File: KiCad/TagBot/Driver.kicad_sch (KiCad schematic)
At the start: 3 parts, among them U2 ZXBM5210-SP

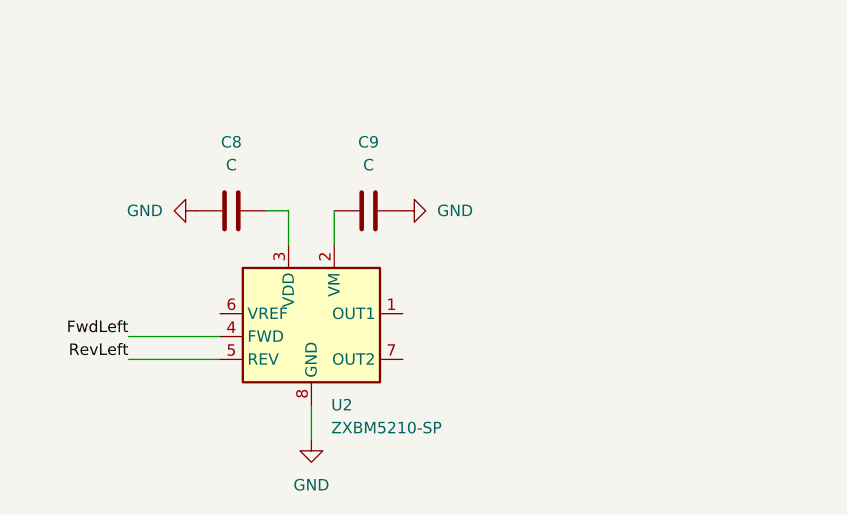
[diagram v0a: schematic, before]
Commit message: kicad and cubeide pin config
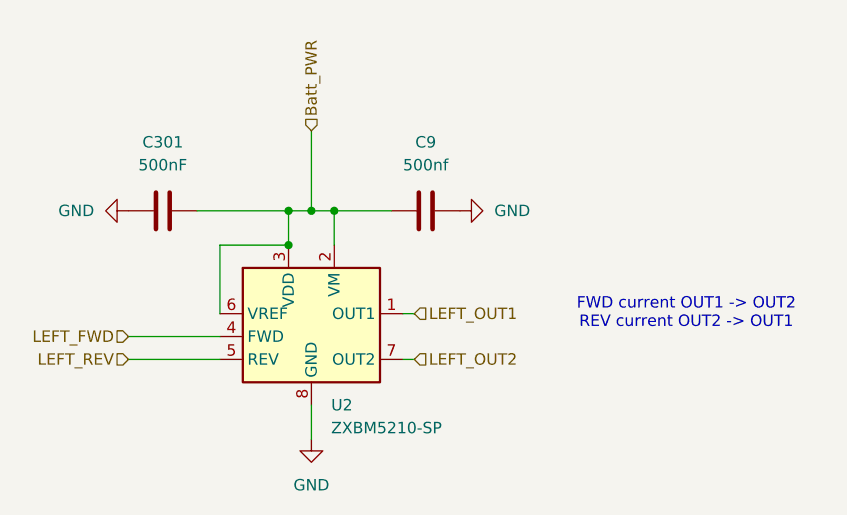
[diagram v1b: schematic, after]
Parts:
- C301: renamed from C8; value C -> 500nF
- C9: value C -> 500nf
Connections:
- net Batt_PWR: now reaches C301.2, U2.3 (VDD)
- net Batt_PWR: now also C9.2, U2.2 (VM), U2.6 (VREF)
- net LEFT_OUT1: now reaches U2.1 (OUT1)
- net LEFT_OUT2: now reaches U2.7 (OUT2)
- net FwdLeft renamed LEFT_FWD
- net RevLeft renamed LEFT_REV
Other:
- note added: "FWD current OUT1 -> OUT2 REV current OUT2 -> OUT1"
- moved on the sheet: C301, C9
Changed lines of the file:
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@@
 	(generator_version "8.0")
 	(paper "A4")
+	(junction
+		(at 138.43 73.66)
+		(diameter 0)
+		(color 0 0 0 0)
+	)
+	(junction
+		(at 143.51 73.66)
+		(diameter 0)
+		(color 0 0 0 0)
+	)
+	(junction
+		(at 140.97 73.66)
+		(diameter 0)
+		(color 0 0 0 0)
+	)
+	(junction
+		(at 138.43 77.47)
+		(diameter 0)
+		(color 0 0 0 0)
+	)
+	(wire
+		(pts
+			(xy 130.81 85.09) (xy 130.81 77.47)
+		)
+		(stroke
+			(width 0)
+			(type default)
+		)
+	)
+	(wire
+		(pts
+			(xy 138.43 73.66) (xy 140.97 73.66)
+		)
+		(stroke
+			(width 0)
+			(type default)
+		)
+	)
 	(wire
 		(pts
@@
 	(wire
 		(pts
+			(xy 152.4 85.09) (xy 151.13 85.09)
+		)
+		(stroke
+			(width 0)
+			(type default)
+		)
+	)
+	(wire
+		(pts
+			(xy 152.4 90.17) (xy 151.13 90.17)
+		)
+		(stroke
+			(width 0)
+			(type default)
+		)
+	)
+	(wire
+		(pts
 			(xy 143.51 73.66) (xy 143.51 77.47)
 		)
@@
 	(wire
 		(pts
+			(xy 130.81 77.47) (xy 138.43 77.47)
+		)
+		(stroke
+			(width 0)
+			(type default)
+		)
+	)
+	(wire
+		(pts
+			(xy 149.86 73.66) (xy 143.51 73.66)
+		)
+		(stroke
+			(width 0)
+			(type default)
+		)
+	)
+	(wire
+		(pts
 			(xy 140.97 95.25) (xy 140.97 99.06)
 		)
@@
 	(wire
 		(pts
-			(xy 138.43 73.66) (xy 135.89 73.66)
-		)
-		(stroke
-			(width 0)
-			(type default)
-		)
-	)
-	(label "RevLeft"
-		(at 120.65 90.17 180)
-		(fields_autoplaced yes)
+			(xy 138.43 73.66) (xy 128.27 73.66)
+		)
+		(stroke
+			(width 0)
+			(type default)
+		)
+	)
+	(wire
+		(pts
+			(xy 140.97 73.66) (xy 143.51 73.66)
+		)
+		(stroke
+			(width 0)
+			(type default)
+		)
+	)
+	(wire
+		(pts
+			(xy 140.97 73.66) (xy 140.97 64.77)
+		)
+		(stroke
+			(width 0)
+			(type default)
+		)
+	)
+	(text "FWD current OUT1 -> OUT2\nREV current OUT2 -> OUT1"
+		(exclude_from_sim no)
+		(at 182.626 85.09 0)
 		(effects
 			(font
 				(size 1.27 1.27)
 			)
-			(justify right bottom)
-		)
-	)
-	(label "FwdLeft"
-		(at 120.65 87.63 180)
+		)
+	)
+	(hierarchical_label "Batt_PWR"
+		(shape input)
+		(at 140.97 64.77 90)
 		(fields_autoplaced yes)
 		(effects
@@
 				(size 1.27 1.27)
 			)
-			(justify right bottom)
+			(justify left)
+		)
+	)
+	(hierarchical_label "LEFT_OUT2"
+		(shape input)
+		(at 152.4 90.17 0)
+		(fields_autoplaced yes)
+		(effects
+			(font
+				(size 1.27 1.27)
+			)
+			(justify left)
+		)
+	)
+	(hierarchical_label "LEFT_FWD"
+		(shape input)
+		(at 120.65 87.63 180)
+		(fields_autoplaced yes)
+		(effects
+			(font
+				(size 1.27 1.27)
+			)
+			(justify right)
+		)
+	)
+	(hierarchical_label "LEFT_REV"
+		(shape input)
+		(at 120.65 90.17 180)
+		(fields_autoplaced yes)
+		(effects
+			(font
+				(size 1.27 1.27)
+			)
+			(justify right)
+		)
+	)
+	(hierarchical_label "LEFT_OUT1"
+		(shape input)
+		(at 152.4 85.09 0)
+		(fields_autoplaced yes)
+		(effects
+			(font
+				(size 1.27 1.27)
+			)
+			(justify left)
 		)
 	)
 	(symbol
 		(lib_id "power:GND")
-		(at 151.13 73.66 90)
+		(at 157.48 73.66 90)
 		(unit 1)
 		(exclude_from_sim no)
@@
 		(fields_autoplaced yes)
 		(property "Reference" "#PWR021"
+			(at 163.83 73.66 0)
+			(effects
+				(font
+					(size 1.27 1.27)
+				)
+				(hide yes)
+			)
+		)
+		(property "Value" "GND"
+			(at 161.29 73.6599 90)
+			(effects
+				(font
+					(size 1.27 1.27)
+				)
+				(justify right)
+			)
+		)
+		(property "Footprint" ""
 			(at 157.48 73.66 0)
 			(effects
@@
 			)
 		)
-		(property "Value" "GND"
-			(at 154.94 73.6599 90)
-			(effects
-				(font
-					(size 1.27 1.27)
-				)
-				(justify right)
-			)
-		)
-		(property "Footprint" ""
-			(at 151.13 73.66 0)
-			(effects
-				(font
-					(size 1.27 1.27)
-				)
-				(hide yes)
-			)
-		)
 		(property "Datasheet" ""
-			(at 151.13 73.66 0)
+			(at 157.48 73.66 0)
 			(effects
 				(font
@@
 		)
 		(property "Description" "Power symbol creates a global label with name \"GND\" , ground"
-			(at 151.13 73.66 0)
+			(at 157.48 73.66 0)
 			(effects
 				(font
@@
 					(unit 1)
 				)
+				(path "/6db08f37-7cb3-4000-93f1-ba0d0ffbeb19/4de9ab2c-d9ad-4c73-a2d5-dcacc317a2ed"
+					(reference "#PWR0303")
+					(unit 1)
+				)
 			)
 		)
@@
 	(symbol
 		(lib_id "Device:C")
-		(at 132.08 73.66 90)
+		(at 124.46 73.66 90)
 		(unit 1)
 		(exclude_from_sim no)
@@
 		(dnp no)
 		(fields_autoplaced yes)
-		(property "Reference" "C8"
-			(at 132.08 66.04 90)
-			(effects
-				(font
-					(size 1.27 1.27)
-				)
-			)
-		)
-		(property "Value" "C"
-			(at 132.08 68.58 90)
+		(property "Reference" "C301"
+			(at 124.46 66.04 90)
+			(effects
+				(font
+					(size 1.27 1.27)
+				)
+			)
+		)
+		(property "Value" "500nF"
+			(at 124.46 68.58 90)
 			(effects
 				(font
@@
 		)
 		(property "Footprint" ""
-			(at 135.89 72.6948 0)
+			(at 128.27 72.6948 0)
 			(effects
 				(font
@@
 		)
 		(property "Datasheet" "~"
-			(at 132.08 73.66 0)
+			(at 124.46 73.66 0)
 			(effects
 				(font
@@
 		)
 		(property "Description" "Unpolarized capacitor"
-			(at 132.08 73.66 0)
+			(at 124.46 73.66 0)
 			(effects
 				(font
@@
 		)
 		(instances
-			(project ""
-				(path "/6db08f37-7cb3-4000-93f1-ba0d0ffbeb19/3ab50834-de79-4373-bbc0-542f9f81e0c6"
-					(reference "C8")
+			(project "TagBot"
+				(path "/6db08f37-7cb3-4000-93f1-ba0d0ffbeb19/4de9ab2c-d9ad-4c73-a2d5-dcacc317a2ed"
+					(reference "C301")
 					(unit 1)
 				)
@@
 					(unit 1)
 				)
+				(path "/6db08f37-7cb3-4000-93f1-ba0d0ffbeb19/4de9ab2c-d9ad-4c73-a2d5-dcacc317a2ed"
+					(reference "U301")
+					(unit 1)
+				)
 			)
 		)
@@
 	(symbol
 		(lib_id "power:GND")
-		(at 128.27 73.66 270)
+		(at 120.65 73.66 270)
 		(unit 1)
 		(exclude_from_sim no)
@@
 		(fields_autoplaced yes)
 		(property "Reference" "#PWR020"
-			(at 121.92 73.66 0)
+			(at 114.3 73.66 0)
 			(effects
 				(font
@@
 		)
 		(property "Value" "GND"
-			(at 124.46 73.6599 90)
+			(at 116.84 73.6599 90)
 			(effects
 				(font
@@
 		)
 		(property "Footprint" ""
-			(at 128.27 73.66 0)
+			(at 120.65 73.66 0)
 			(effects
 				(font
@@
 		)
 		(property "Datasheet" ""
-			(at 128.27 73.66 0)
+			(at 120.65 73.66 0)
 			(effects
 				(font
@@
 		)
 		(property "Description" "Power symbol creates a global label with name \"GND\" , ground"
-			(at 128.27 73.66 0)
+			(at 120.65 73.66 0)
 			(effects
 				(font
@@
 					(unit 1)
 				)
+				(path "/6db08f37-7cb3-4000-93f1-ba0d0ffbeb19/4de9ab2c-d9ad-4c73-a2d5-dcacc317a2ed"
+					(reference "#PWR0301")
+					(unit 1)
+				)
 			)
 		)
@@
 	(symbol
 		(lib_id "Device:C")
-		(at 147.32 73.66 270)
+		(at 153.67 73.66 270)
 		(unit 1)
 		(exclude_from_sim no)
@@
 		(fields_autoplaced yes)
 		(property "Reference" "C9"
-			(at 147.32 66.04 90)
-			(effects
-				(font
-					(size 1.27 1.27)
-				)
-			)
-		)
-		(property "Value" "C"
-			(at 147.32 68.58 90)
+			(at 153.67 66.04 90)
+			(effects
+				(font
+					(size 1.27 1.27)
+				)
+			)
+		)
+		(property "Value" "500nf"
+			(at 153.67 68.58 90)
 			(effects
 				(font
@@
 		)
 		(property "Footprint" ""
-			(at 143.51 74.6252 0)
+			(at 149.86 74.6252 0)
 			(effects
 				(font
@@
 		)
 		(property "Datasheet" "~"
-			(at 147.32 73.66 0)
+			(at 153.67 73.66 0)
 			(effects
 				(font
@@
 		)
 		(property "Description" "Unpolarized capacitor"
-			(at 147.32 73.66 0)
+			(at 153.67 73.66 0)
 			(effects
 				(font
@@
 				(path "/6db08f37-7cb3-4000-93f1-ba0d0ffbeb19/3ab50834-de79-4373-bbc0-542f9f81e0c6"
 					(reference "C9")
+					(unit 1)
+				)
+				(path "/6db08f37-7cb3-4000-93f1-ba0d0ffbeb19/4de9ab2c-d9ad-4c73-a2d5-dcacc317a2ed"
+					(reference "C302")
 					(unit 1)
 				)
@@
 		(dnp no)
 		(fields_autoplaced yes)
-		(property "Reference" "#PWR019"
+		(property "Reference" "#PWR0302"
 			(at 140.97 105.41 0)
 			(effects
@@
 		)
 		(instances
-			(project ""
-				(path "/6db08f37-7cb3-4000-93f1-ba0d0ffbeb19/3ab50834-de79-4373-bbc0-542f9f81e0c6"
-					(reference "#PWR019")
-					(unit 1)
-				)
+			(project "TagBot"
+				(path "/6db08f37-7cb3-4000-93f1-ba0d0ffbeb19/4de9ab2c-d9ad-4c73-a2d5-dcacc317a2ed"
+					(reference "#PWR0302")
+					(unit 1)
+				)
